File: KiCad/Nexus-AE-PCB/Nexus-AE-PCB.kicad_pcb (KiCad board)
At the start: 2 copper layers, 50 x 100 mm, 163 parts, among them CN1 I2C_IN, CN2 I2C_OUT, J1 Conn_01x20_Socket, J2 Conn_01x20_Socket, J3 AE_BUS, J4 Inputs, J5 Outputs, J6 SPI, J7 SD_CONN, Q1 AO3401, Q2 2N3904, Q3 2N3904, SW1 SW_Push, SW2 SW_Push, U1 ATmega4809-A, U2 MCP6002T-I_MS, U3 Driver_LED_PCA9633PW,118, U4 MCP6002T-I_MS, U5 MCP6002T-I_MS, U6 MCP6002T-I_MS, U7 USBLC6-2SC6, U8 MCP6002T-I_MS, U9 74xGxx_MDD_74AHCT1G125GV

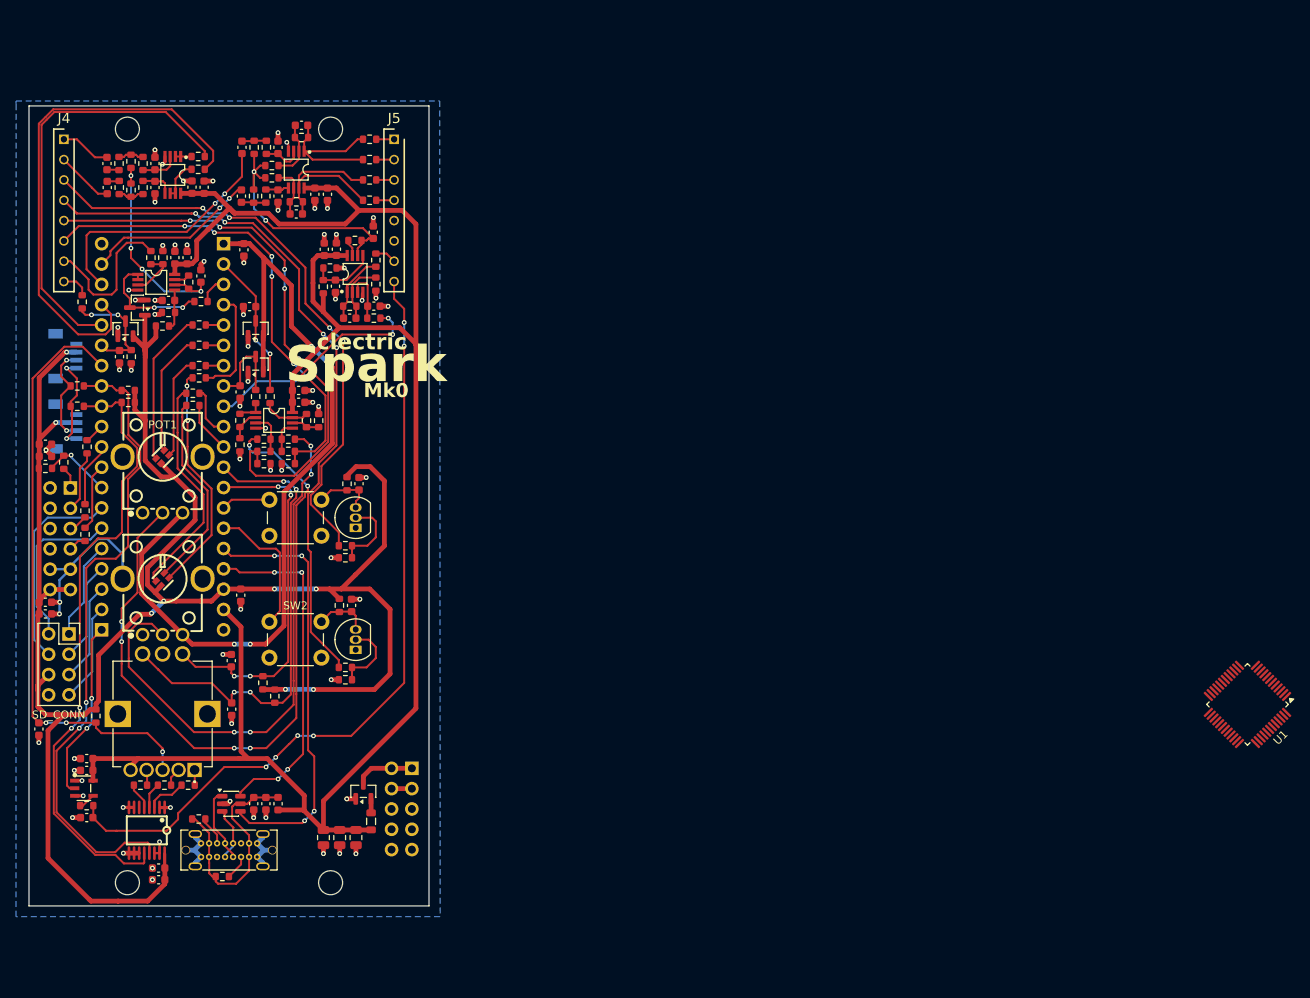
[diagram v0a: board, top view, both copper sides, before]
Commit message: PCB and schmeatic are both approx 90% complete
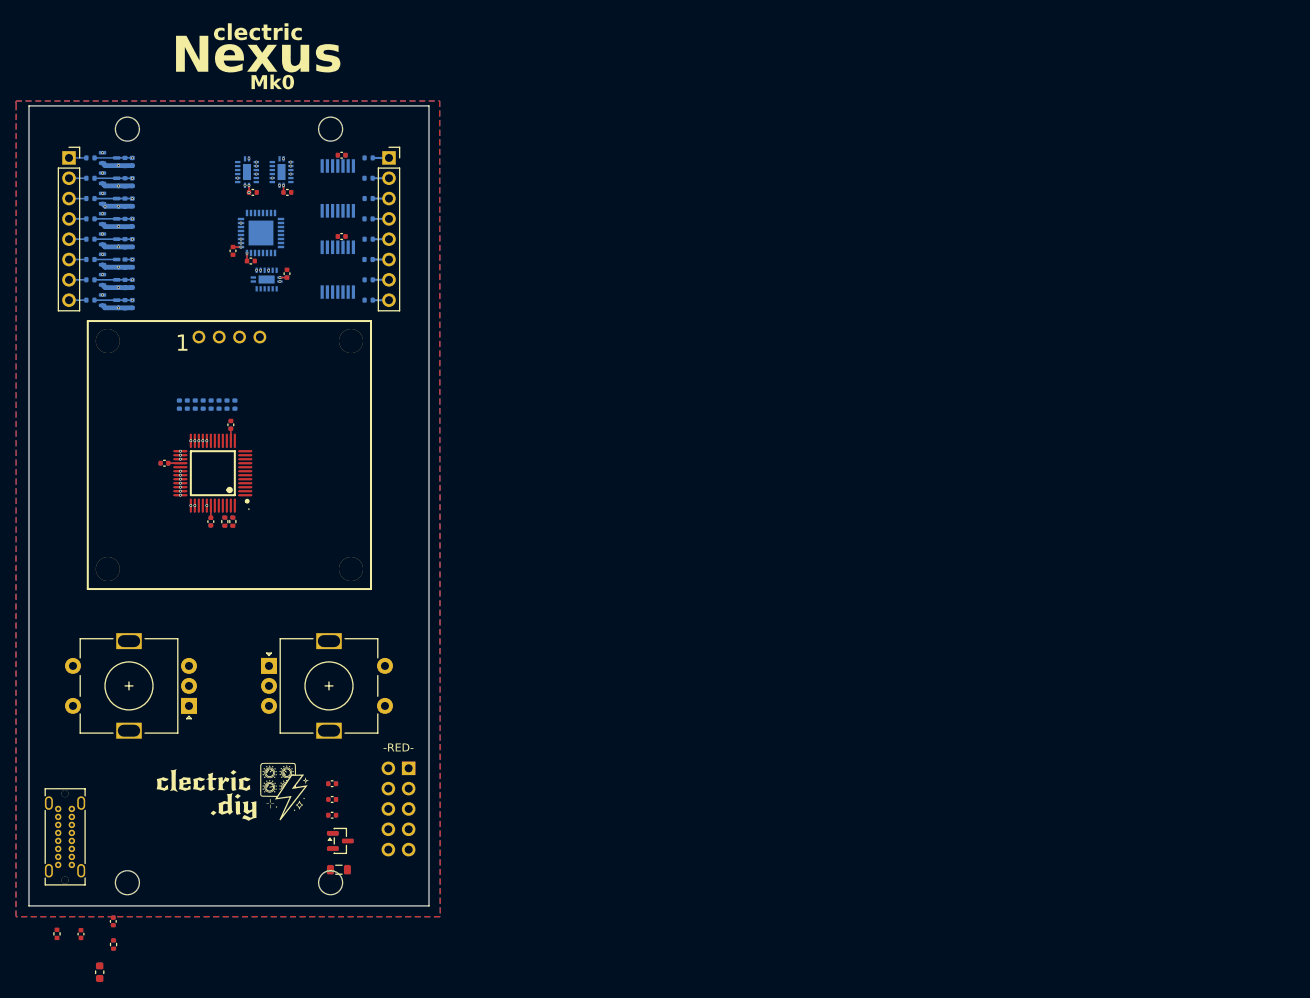
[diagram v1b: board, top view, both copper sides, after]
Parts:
- removed C24, C30, C36, C40, C42, C45, C50, C52: 10uF, Capacitor_SMD:C_0603_1608Metric
- removed C25, C26, C38: 1nF, Capacitor_SMD:C_0603_1608Metric
- removed C27, C28: 680pF, Capacitor_SMD:C_0603_1608Metric
- removed C29, C33, C34, C35, C39, C41, C43, C44, C48, C49, C51: 100nF, Capacitor_SMD:C_0603_1608Metric
- removed C37: 10nF, Capacitor_SMD:C_0603_1608Metric
- removed C46: 100pF, Capacitor_SMD:C_0603_1608Metric
- removed C47: 10pF, Capacitor_SMD:C_0603_1608Metric
- removed CN1: I2C_IN, clectric-diy:Connector_JST_BM04B-SRSS-TBT-LF-SN
- removed CN2: I2C_OUT, clectric-diy:Connector_JST_BM04B-SRSS-TBT-LF-SN
- removed J4: Inputs, clectric-diy:Connector_PinSocket-1x08-P2.54mm-H8.5mm_Preci-Dip_801-87-008-10-005101
- removed J5: Outputs, clectric-diy:Connector_PinSocket-1x08-P2.54mm-H8.5mm_Preci-Dip_801-87-008-10-005101
- removed J6: SPI, Connector_PinHeader_2.54mm:PinHeader_2x06_P2.54mm_Vertical
- removed J7: SD_CONN, Connector_PinSocket_2.54mm:PinSocket_2x04_P2.54mm_Vertical
- removed LED1, LED2: A-SP1943B1GHR6C-C01-2T, clectric-diy:LED_ARGB_Amicc_A-SP1943B1GHR6C-C01-2T
- removed POT1, POT2: RK09K1130D62, clectric-diy:Potentiometer_THT_Alps_RK09K1130D62
- removed Q2, Q3: 2N3904, Package_TO_SOT_THT:TO-92_Inline
- removed R37, R38, R43, R44, R45, R46, R55, R65, R68, R72, R78: 10K, Resistor_SMD:R_0603_1608Metric
- removed R39, R40, R49, R50, R51, R52, R63, R69, R75: 1K, Resistor_SMD:R_0603_1608Metric
- removed R41, R42, R53, R54, R70, R71: 100K, Resistor_SMD:R_0603_1608Metric
- removed R47, R48: 15K, Resistor_SMD:R_0603_1608Metric
- removed R56: 20K, Resistor_SMD:R_0603_1608Metric
- removed R62, R74, R76, R77: 100R, Resistor_SMD:R_0603_1608Metric
- removed R64, R67: 56K, Resistor_SMD:R_0603_1608Metric
- removed R66: 12.7K, Resistor_SMD:R_0603_1608Metric
- removed R73: 470R, Resistor_SMD:R_0603_1608Metric
- removed R79, R80, R81, R82: 47R, Resistor_SMD:R_0603_1608Metric
- removed SW1, SW2: SW_Push, Button_Switch_THT:SW_PUSH_6mm
- removed U8: MCP6002T-I_MS, clectric-diy:Amplifier_Operational_Microchip_MCP6002T-I_MS
- removed U9: 74xGxx_MDD_74AHCT1G125GV, clectric-diy:74xGxx_MDD_74AHCT1G125GV
- added D6: BAT54SW, Package_TO_SOT_SMD:SOT-323_SC-70, B.Cu at (88.5, 65.3)
- added D7: BAT54SW, Package_TO_SOT_SMD:SOT-323_SC-70, B.Cu at (88.5, 67.9)
- added D8: BAT54SW, Package_TO_SOT_SMD:SOT-323_SC-70, B.Cu at (88.5, 70.4)
- added ENC1: RotaryEncoder_Switch, Rotary_Encoder:RotaryEncoder_Alps_EC11E-Switch_Vertical_H20mm, F.Cu at (90.9, 118.6)
- added ENC2: RotaryEncoder_Switch, Rotary_Encoder:RotaryEncoder_Alps_EC11E-Switch_Vertical_H20mm, F.Cu at (115.9, 118.6)
- added OLED1: HS13L03W2C01, clectric-diy:OLED-TH_L35.4-W33.5_HS13L03W2C01, F.Cu at (103.4, 75.0)
- C1: value 100uF -> 100nF; footprint Capacitor_SMD:C_0805_2012Metric -> Capacitor_SMD:C_0402_1005Metric
- C10, C21, C5, C6: footprint Capacitor_SMD:C_0603_1608Metric -> Capacitor_SMD:C_0402_1005Metric
- C11, C7: value 10nF -> 100nF; footprint Capacitor_SMD:C_0603_1608Metric -> Capacitor_SMD:C_0402_1005Metric
- C12, C13, C14: value 10nF -> 100pF; footprint Capacitor_SMD:C_0603_1608Metric -> Capacitor_SMD:C_0402_1005Metric; moved to B.Cu
- C15: value 10uF -> 100pF; footprint Capacitor_SMD:C_0603_1608Metric -> Capacitor_SMD:C_0402_1005Metric; moved to B.Cu
- C16: value 100nF -> 100pF; footprint Capacitor_SMD:C_0603_1608Metric -> Capacitor_SMD:C_0402_1005Metric; moved to B.Cu
- C17, C18: value 1uF -> 100pF; footprint Capacitor_SMD:C_0603_1608Metric -> Capacitor_SMD:C_0402_1005Metric; moved to B.Cu
- C19: value 220pF -> 100pF; footprint Capacitor_SMD:C_0603_1608Metric -> Capacitor_SMD:C_0402_1005Metric; moved to B.Cu
- C2: value 10uF -> 100nF; footprint Capacitor_SMD:C_0805_2012Metric -> Capacitor_SMD:C_0402_1005Metric
- C20: value 220pF -> 100nF; footprint Capacitor_SMD:C_0603_1608Metric -> Capacitor_SMD:C_0402_1005Metric
- C22, C23, C9: value 10uF -> 100nF; footprint Capacitor_SMD:C_0603_1608Metric -> Capacitor_SMD:C_0402_1005Metric
- C3: footprint Capacitor_SMD:C_0805_2012Metric -> Capacitor_SMD:C_0402_1005Metric
- C4: value 10uF -> 100uF; footprint Capacitor_SMD:C_0603_1608Metric -> Capacitor_SMD:C_0402_1005Metric
- C8: value 100nF -> 10uF; footprint Capacitor_SMD:C_0603_1608Metric -> Capacitor_SMD:C_0402_1005Metric
- D1, D2, D4, D5: value BAT54S -> BAT54SW; footprint Package_TO_SOT_SMD:SOT-23 -> Package_TO_SOT_SMD:SOT-323_SC-70; moved to B.Cu
- D3: value RotaryEncoder_Switch_Bourns_PEL12T-4225S-S1024 -> BAT54SW; footprint clectric-diy:RotaryEncoder_Switch_Bourns_PEL12T-4225S-S1024 -> Package_TO_SOT_SMD:SOT-323_SC-70; moved to B.Cu
- G***: moved to F.Cu
- J1: value Conn_01x20_Socket -> AE_BUS; footprint clectric-diy:Connector_PinSocket-1x20-P2.54mm-H1.27mm_Mill-Max_315-13-120-41-004000 -> Connector_PinHeader_2.54mm:PinHeader_2x05_P2.54mm_Vertical
- J2: value Conn_01x20_Socket -> Conn_01x08_Socket; footprint clectric-diy:Connector_PinSocket-1x20-P2.54mm-H1.27mm_Mill-Max_315-13-120-41-004000 -> Connector_PinSocket_2.54mm:PinSocket_1x08_P2.54mm_Vertical; moved to F.Cu
- J3: value AE_BUS -> Conn_01x08_Socket; footprint Connector_PinHeader_2.54mm:PinHeader_2x05_P2.54mm_Vertical -> Connector_PinSocket_2.54mm:PinSocket_1x08_P2.54mm_Vertical; moved to F.Cu
- R1, R11, R13, R19, R2, R23, R3, R31, R7: value 10K -> 1k; footprint Resistor_SMD:R_0603_1608Metric -> Resistor_SMD:R_0402_1005Metric; moved to B.Cu
- R10: value 47R -> 56K; footprint Resistor_SMD:R_0603_1608Metric -> Resistor_SMD:R_0402_1005Metric
- R12, R24: value 1K -> 100k; footprint Resistor_SMD:R_0603_1608Metric -> Resistor_SMD:R_0402_1005Metric; moved to B.Cu
- R14, R21: value 100K -> 100k; footprint Resistor_SMD:R_0603_1608Metric -> Resistor_SMD:R_0402_1005Metric; moved to B.Cu
- R15, R22, R25, R26: value 10K -> 100k; footprint Resistor_SMD:R_0603_1608Metric -> Resistor_SMD:R_0402_1005Metric; moved to B.Cu
- R16: value 47R -> 100k; footprint Resistor_SMD:R_0603_1608Metric -> Resistor_SMD:R_0402_1005Metric; moved to B.Cu
- R17: value 330R -> 1k; footprint Resistor_SMD:R_0603_1608Metric -> Resistor_SMD:R_0402_1005Metric; moved to B.Cu
- R18, R8: value 47R -> 1k; footprint Resistor_SMD:R_0603_1608Metric -> Resistor_SMD:R_0402_1005Metric; moved to B.Cu
- R20, R35, R36, R4, R5, R6: value 100K -> 1k; footprint Resistor_SMD:R_0603_1608Metric -> Resistor_SMD:R_0402_1005Metric; moved to B.Cu
- R27: value 4K7 -> 4.7k; footprint Resistor_SMD:R_0603_1608Metric -> Resistor_SMD:R_0402_1005Metric
- R28: value 680R -> 4.7k; footprint Resistor_SMD:R_0603_1608Metric -> Resistor_SMD:R_0402_1005Metric
- R29, R30: value 470R -> 1k; footprint Resistor_SMD:R_0603_1608Metric -> Resistor_SMD:R_0402_1005Metric; moved to B.Cu
- R32: value 4K7 -> 1k; footprint Resistor_SMD:R_0603_1608Metric -> Resistor_SMD:R_0402_1005Metric; moved to B.Cu
- R33, R34: value 150K -> 1k; footprint Resistor_SMD:R_0603_1608Metric -> Resistor_SMD:R_0402_1005Metric; moved to B.Cu
- R9: value 330R -> 56K; footprint Resistor_SMD:R_0603_1608Metric -> Resistor_SMD:R_0402_1005Metric
- U1: value ATmega4809-A -> ATMEGA4809-AUR; footprint Package_QFP:TQFP-48_7x7mm_P0.5mm -> clectric-diy:TQFP-48_L7.0-W7.0-P0.50-LS9.0-BL
- U2, U4: value MCP6002T-I_MS -> 74HC4053BQ,115; footprint clectric-diy:Amplifier_Operational_Microchip_MCP6002T-I_MS -> clectric-diy:DHVQFN-16_L3.5-W2.5-P0.50-BL-EP; moved to B.Cu
- U3: value Driver_LED_PCA9633PW,118 -> 74HC4053BQ,115; footprint clectric-diy:TSSOP-16_L5.0-W4.4-P0.64-LS6.4-BL -> clectric-diy:DHVQFN-16_L3.5-W2.5-P0.50-BL-EP; moved to B.Cu
- U5: value MCP6002T-I_MS -> ADG2188BCPZ-REEL7; footprint clectric-diy:Amplifier_Operational_Microchip_MCP6002T-I_MS -> clectric-diy:LFCSP-32_L5.0-W5.0-P0.50-TL-EP3.1; moved to B.Cu
- U6: value MCP6002T-I_MS -> MCP6004T-I/ST; footprint clectric-diy:Amplifier_Operational_Microchip_MCP6002T-I_MS -> clectric-diy:TSSOP-14_L5.0-W4.4-P0.65-LS6.4-BL; moved to B.Cu
- U7: value USBLC6-2SC6 -> MCP6004T-I/ST; footprint Package_TO_SOT_SMD:SOT-23-6 -> clectric-diy:TSSOP-14_L5.0-W4.4-P0.65-LS6.4-BL; moved to B.Cu
- moved U1 132.5 mm to (101.4, 92.0), turned to 90 degrees
- moved U3 84.0 mm to (109.9, 54.4), turned to 90 degrees
- moved C15 80.7 mm to (91.3, 60.7), turned to -90 degrees
- moved C16 79.7 mm to (91.3, 63.3), turned to -90 degrees
- moved R10 78.2 mm to (88.9, 151.0), turned to 90 degrees
- moved J3 76.4 mm to (123.4, 52.6), turned to 0 degrees
- moved R9 73.2 mm to (81.9, 149.6), turned to 90 degrees
- moved C7 70.6 mm to (84.9, 149.7), turned to 90 degrees
- moved C5 69.6 mm to (116.3, 132.8), turned to 0 degrees
- moved J1 69.5 mm to (125.8, 128.9)
- moved C8 68.9 mm to (88.9, 148.1), turned to 90 degrees
- moved U7 68.1 mm to (117.0, 66.6)
- moved C13 67.1 mm to (91.3, 55.7)
- moved C14 66.9 mm to (91.3, 58.2), turned to -90 degrees
- moved R15 66.7 mm to (86.1, 57.7)
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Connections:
- C1 pad 1: +5V -> GND
- C1 pad 2: GND -> +5VA
- C10 pad 1: SW2 -> +5V
- C11 pad 1: POT2 -> +5V
- C12 pad 1: ENC_A -> AE_IN_A
- C13 pad 1: ENC_B -> AE_IN_B
- C14 pad 1: GND -> AE_IN_C
- C14 pad 2: ENC_CLICK -> GND
- C15 pad 1: +3.3V -> AE_IN_D
- C16 pad 1: +3.3V -> AE_IN_E
- C17 pad 1: AUDIO_AE_IN_1 -> AE_IN_F
- C17 pad 2: Net-(C17-Pad2) -> GND
- C18 pad 1: AUDIO_AE_IN_2 -> AE_IN_G
- C18 pad 2: Net-(C18-Pad2) -> GND
- C19 pad 1: Net-(U4A-+) -> AE_IN_H
- C2 pad 1: +5V -> GND
- C2 pad 2: GND -> +5VA
- C20 pad 1: Net-(U4B-+) -> GND
- C20 pad 2: GND -> +5V
- C21 pad 1: GND -> +5V
- C21 pad 2: +5V -> GND
- C22 pad 1: GND -> +5V
- C22 pad 2: +5V -> GND
- C23 pad 1: Net-(C23-Pad1) -> +5VA
- C23 pad 2: AUDIO_OUT_1 -> GND
- C3 pad 1: +5V -> GND
- C3 pad 2: GND -> +5V
- C4 pad 1: GND -> +5V
- C4 pad 2: +3.3V -> GND
- C5 pad 1: GND -> +5V
- C5 pad 2: +3.3VA -> GND
- C6 pad 1: SW1 -> +5V
- C7 pad 1: POT1 -> Net-(C7-Pad1)
- C8 pad 1: +5V -> Net-(C7-Pad1)
- C9 pad 1: GND -> +5V
- C9 pad 2: +5V -> GND
- D1 pad 2: +3.3VA -> +5V
- D1 pad 3: POT1 -> AE_IN_A
- D2 pad 2: +3.3VA -> +5V
- D2 pad 3: POT2 -> AE_IN_B
- D3 pad 1: Net-(D3-Pad1) -> GND
- D3 pad 2: Net-(D3-Pad2) -> +5V
- D3 pad 3: ENC_CLICK -> AE_IN_C
- D4 pad 1: +3.3V -> GND
- D4 pad 2: GND -> +5V
- D4 pad 3: Net-(D4-COM) -> AE_IN_D
- D5 pad 2: +3.3V -> +5V
- D5 pad 3: D14 -> AE_IN_E
- F1 pad 2: Net-(U7-VBUS) -> Net-(C7-Pad1)
- J1 pad 1: +3.3VA -> /Power Regulation/VCC_RAW
- J1 pad 10: LED2_B -> unconnected-(J1-Pin_10-Pad10)
- J1 pad 2: POT2 -> /Power Regulation/VCC_RAW
- J1 pad 3: A1 -> GND
- J1 pad 4: LED2_R -> GND
- J1 pad 5: LED1_B -> unconnected-(J1-Pin_5-Pad5)
- J1 pad 6: LED1_G -> unconnected-(J1-Pin_6-Pad6)
- J1 pad 7: LED1_R -> unconnected-(J1-Pin_7-Pad7)
- J1 pad 8: POT1 -> unconnected-(J1-Pin_8-Pad8)
- J1 pad 9: A7 -> unconnected-(J1-Pin_9-Pad9)
- J2 pad 1: D0 -> AE_IN_A_RAW
- J2 pad 2: SD_D3 -> AE_IN_B_RAW
- J2 pad 3: SD_D2 -> AE_IN_C_RAW
- J2 pad 4: SD_D1 -> AE_IN_D_RAW
- J2 pad 5: SD_D0 -> AE_IN_E_RAW
- J2 pad 6: SD_CMD -> AE_IN_F_RAW
- J2 pad 7: SD_CK -> AE_IN_G_RAW
- J2 pad 8: SPI_CS -> AE_IN_H_RAW
- J3 pad 1: /Power Regulation/VCC_RAW -> AE_OUT_1
- J3 pad 2: /Power Regulation/VCC_RAW -> AE_OUT_2
- J3 pad 3: GND -> AE_OUT_3
- J3 pad 4: GND -> AE_OUT_4
- J3 pad 5: unconnected-(J3-Pin_5-Pad5) -> AE_OUT_5
- J3 pad 6: unconnected-(J3-Pin_6-Pad6) -> AE_OUT_6
- J3 pad 7: unconnected-(J3-Pin_7-Pad7) -> AE_OUT_7
- J3 pad 8: unconnected-(J3-Pin_8-Pad8) -> AE_OUT_8
- R1 pad 1: POT1_CV -> AE_OUT_1
- R1 pad 2: GND -> DEST_1_BUF
- R10 pad 1: LED1_B -> Net-(C7-Pad1)
- R10 pad 2: Net-(LED1-Pad4) -> Net-(USB1-CC2)
- R11 pad 1: Net-(U2A--) -> AE_IN_A_RAW
- R11 pad 2: Net-(R11-Pad2) -> AE_IN_A
- R12 pad 1: Net-(R11-Pad2) -> AE_IN_A
- R12 pad 2: POT1 -> GND
- R13 pad 1: POT2_CV -> AE_IN_B_RAW
- R13 pad 2: GND -> AE_IN_B
- R14 pad 1: Net-(U2B-+) -> AE_IN_B
- R14 pad 2: POT2_CV -> GND
- R15 pad 1: SW2_CV -> AE_IN_C_RAW
- R15 pad 2: Net-(Q3-B) -> AE_IN_C
- R16 pad 1: LED2_G -> AE_IN_C
- R16 pad 2: Net-(LED2-Pad1) -> GND
- R17 pad 1: LED2_R -> AE_IN_D_RAW
- R17 pad 2: Net-(LED2-Pad2) -> AE_IN_D
- R18 pad 1: LED2_B -> AE_IN_D
- R18 pad 2: Net-(LED2-Pad4) -> GND
- R19 pad 1: +3.3V -> AE_IN_E_RAW
- R19 pad 2: SW2 -> AE_IN_E
- R2 pad 1: SW1_CV -> AE_OUT_2
- R2 pad 2: Net-(Q2-B) -> DEST_2_BUF
- R20 pad 1: Net-(POT2-Pad2) -> AE_IN_E
- R20 pad 2: Net-(U2B-+) -> GND
- R21 pad 1: Net-(Q3-B) -> AE_IN_F_RAW
- R21 pad 2: GND -> AE_IN_F
- R22 pad 1: Net-(U2B--) -> AE_IN_F
- R23 pad 1: Net-(U2B--) -> AE_IN_G_RAW
- R23 pad 2: Net-(R23-Pad2) -> AE_IN_G
- R24 pad 1: Net-(R23-Pad2) -> AE_IN_G
- R24 pad 2: POT2 -> GND
- R25 pad 1: +3.3V -> AE_IN_H_RAW
- R25 pad 2: ENC_A -> AE_IN_H
- R26 pad 1: +3.3V -> AE_IN_H
- R26 pad 2: ENC_B -> GND
- R27 pad 1: +3.3V -> +5V
- R28 pad 1: Net-(D3-Pad1) -> +5V
- R28 pad 2: ENC_LED_RED -> I2C_SCL
- R29 pad 1: Net-(D3-Pad2) -> MCU_GEN_A
- R29 pad 2: ENC_LED_GREEN -> /Microchip ATMega4809/MCU_GEN_A_RAW
- R3 pad 1: +3.3V -> AE_OUT_3
- R3 pad 2: SW1 -> DEST_3_BUF
- R30 pad 1: ENC_LED_BLUE -> MCU_GEN_B
- R30 pad 2: Net-(D3-Pad4) -> /Microchip ATMega4809/MCU_GEN_B_RAW
- R31 pad 1: +3.3V -> MCU_GEN_C
- R31 pad 2: ENC_CLICK -> /Microchip ATMega4809/MCU_GEN_C_RAW
- R32 pad 1: +3.3V -> MCU_GEN_D
- R32 pad 2: I2C_SCL -> /Microchip ATMega4809/MCU_GEN_D_RAW
- R33 pad 1: Net-(C17-Pad2) -> MCU_GEN_E
- R33 pad 2: Net-(R33-Pad2) -> /Microchip ATMega4809/MCU_GEN_E_RAW
- R34 pad 1: Net-(C18-Pad2) -> MCU_GEN_F
- R34 pad 2: Net-(R34-Pad2) -> /Microchip ATMega4809/MCU_GEN_F_RAW
- R35 pad 1: Net-(R33-Pad2) -> MCU_GEN_G
- R35 pad 2: VREF_1V65 -> /Microchip ATMega4809/MCU_GEN_G_RAW
- R36 pad 1: Net-(R34-Pad2) -> MCU_GEN_H
- R36 pad 2: VREF_1V65 -> /Microchip ATMega4809/MCU_GEN_H_RAW
- R4 pad 1: Net-(U2A-+) -> AE_OUT_4
- R4 pad 2: POT1_CV -> DEST_4_BUF
- R5 pad 1: Net-(Q2-B) -> AE_OUT_5
- R5 pad 2: GND -> DEST_5_BUF
- R6 pad 1: Net-(POT1-Pad2) -> AE_OUT_6
- R6 pad 2: Net-(U2A-+) -> DEST_6_BUF
- R7 pad 1: Net-(U2A--) -> AE_OUT_7
- R7 pad 2: GND -> DEST_7_BUF
- R8 pad 1: LED1_G -> AE_OUT_8
- R8 pad 2: Net-(LED1-Pad1) -> DEST_8_BUF
- R9 pad 1: LED1_R -> Net-(C7-Pad1)
- R9 pad 2: Net-(LED1-Pad2) -> Net-(USB1-CC1)
- U1 pad 10: unconnected-(U1-PC0-Pad10) -> /Microchip ATMega4809/MCU_GEN_A_RAW
- U1 pad 11: unconnected-(U1-PC1-Pad11) -> /Microchip ATMega4809/MCU_GEN_B_RAW
- U1 pad 12: unconnected-(U1-PC2-Pad12) -> /Microchip ATMega4809/MCU_GEN_C_RAW
- U1 pad 13: unconnected-(U1-PC3-Pad13) -> /Microchip ATMega4809/MCU_GEN_D_RAW
- U1 pad 16: unconnected-(U1-PC4-Pad16) -> /Microchip ATMega4809/MCU_GEN_E_RAW
- U1 pad 17: unconnected-(U1-PC5-Pad17) -> /Microchip ATMega4809/MCU_GEN_F_RAW
- U1 pad 18: unconnected-(U1-PC6-Pad18) -> /Microchip ATMega4809/MCU_GEN_G_RAW
- U1 pad 19: unconnected-(U1-PC7-Pad19) -> /Microchip ATMega4809/MCU_GEN_H_RAW
- U1 pad 20: AE_SOCKET_1 -> AE_IN_A
- U1 pad 21: AE_SOCKET_2 -> AE_IN_B
- U1 pad 22: AE_SOCKET_3 -> AE_IN_C
- U1 pad 23: AE_SOCKET_4 -> AE_IN_D
- U1 pad 24: AE_SOCKET_5 -> AE_IN_E
- U1 pad 25: AE_SOCKET_6 -> AE_IN_F
- U1 pad 26: AE_SOCKET_7 -> AE_IN_G
- U1 pad 27: AE_SOCKET_8 -> AE_IN_H
- U1 pad 30: unconnected-(U1-PE0-Pad30) -> SRC_SEL_A
- U1 pad 31: unconnected-(U1-PE1-Pad31) -> SRC_SEL_B
- U1 pad 32: unconnected-(U1-PE2-Pad32) -> SRC_SEL_C
- U1 pad 33: unconnected-(U1-PE3-Pad33) -> SRC_SEL_D
- U1 pad 34: unconnected-(U1-PF0-Pad34) -> SRC_SEL_E
- U1 pad 35: unconnected-(U1-PF1-Pad35) -> SRC_SEL_F
- U1 pad 36: unconnected-(U1-PF2-Pad36) -> SRC_SEL_G
- U1 pad 37: unconnected-(U1-PF3-Pad37) -> SRC_SEL_H
- U1 pad 38: unconnected-(U1-PF4-Pad38) -> MATRIX_RESET
- U1 pad 4: unconnected-(U1-PB0-Pad4) -> ENC_1_A
- U1 pad 41: unconnected-(U1-UPDI-Pad41) -> UPDI
- U1 pad 42: +5V -> +5VA
- U1 pad 46: unconnected-(U1-PA2-Pad46) -> I2C_SDA
- U1 pad 47: unconnected-(U1-PA3-Pad47) -> I2C_SCL
- U1 pad 5: unconnected-(U1-PB1-Pad5) -> ENC_1_B
- U1 pad 6: unconnected-(U1-PB2-Pad6) -> ENC_1_SW
- U1 pad 7: unconnected-(U1-PB3-Pad7) -> ENC_2_A
- U1 pad 8: unconnected-(U1-PB4-Pad8) -> ENC_2_B
- U1 pad 9: unconnected-(U1-PB5-Pad9) -> ENC_2_SW
- U2 pad 1: Net-(R11-Pad2) -> MCU_GEN_C
- U2 pad 2: Net-(U2A--) -> AE_IN_C
- U2 pad 3: Net-(U2A-+) -> MCU_GEN_B
- U2 pad 4: GND -> SRC_B
- U2 pad 5: Net-(U2B-+) -> AE_IN_B
- U2 pad 6: Net-(U2B--) -> GND
- U2 pad 7: Net-(R23-Pad2) -> GND
- U2 pad 8: +5V -> GND
- U3 pad 1: GND -> MCU_GEN_D
- U3 pad 10: GND -> SRC_SEL_E
- U3 pad 11: GND -> SRC_SEL_D
- U3 pad 12: I2C_SCL -> AE_IN_E
- U3 pad 13: I2C_SDA -> MCU_GEN_E
- U3 pad 14: GND -> SRC_E
- U3 pad 15: GND -> SRC_D
- U3 pad 16: +3.3V -> +5V
- U3 pad 2: GND -> AE_IN_D
- U3 pad 3: ENC_LED_RED -> MCU_GEN_F
- U3 pad 4: ENC_LED_GREEN -> SRC_F
- U3 pad 5: ENC_LED_BLUE -> AE_IN_F
- U3 pad 6: unconnected-(U3-LED3-Pad6) -> GND
- U3 pad 9: GND -> SRC_SEL_F
- U4 pad 1: Net-(U4A--) -> MCU_GEN_G
- U4 pad 2: Net-(U4A--) -> AE_IN_G
- U4 pad 3: Net-(U4A-+) -> GND
- U4 pad 5: Net-(U4B-+) -> GND
- U4 pad 6: Net-(U4B--) -> GND
- U4 pad 7: Net-(U4B--) -> GND
- U4 pad 8: +5V -> GND
- U5 pad 1: Net-(C27-Pad1) -> GND
- U5 pad 2: Net-(U5A--) -> unconnected-(U5-DNC-Pad2)
- U5 pad 3: Net-(U5A-+) -> SRC_A
- U5 pad 4: GND -> SRC_B
- U5 pad 5: Net-(U5B-+) -> SRC_C
- U5 pad 6: Net-(U5B--) -> SRC_D
- U5 pad 7: Net-(C28-Pad1) -> SRC_E
- U5 pad 8: +5V -> SRC_F
- U6 pad 1: Net-(D4-COM) -> DEST_1_BUF
- U6 pad 2: Net-(D4-COM) -> DEST_1_BUF
- U6 pad 3: Net-(U6A-+) -> DEST_1
- U6 pad 4: GND -> +5V
- U6 pad 5: Net-(U6B-+) -> DEST_2
- U6 pad 6: VREF_1V65 -> DEST_2_BUF
- U6 pad 7: Net-(R62-Pad1) -> DEST_2_BUF
- U6 pad 8: +5V -> DEST_3_BUF
- U7 pad 1: Net-(U7-I/O1-Pad1) -> DEST_5_BUF
- U7 pad 2: GND -> DEST_5_BUF
- U7 pad 3: Net-(U7-I/O2-Pad3) -> DEST_5
- U7 pad 4: USB_D- -> +5V
- U7 pad 5: Net-(U7-VBUS) -> DEST_6
- U7 pad 6: USB_D+ -> DEST_6_BUF
- USB1 pad A4: Net-(U7-VBUS) -> Net-(C7-Pad1)
- USB1 pad A6: Net-(U7-I/O1-Pad1) -> Net-(USB1-D+-PadA6)
- USB1 pad A7: Net-(U7-I/O2-Pad3) -> Net-(USB1-D--PadA7)
- USB1 pad A9: Net-(U7-VBUS) -> Net-(C7-Pad1)
- USB1 pad B4: Net-(U7-VBUS) -> Net-(C7-Pad1)
- USB1 pad B6: Net-(U7-I/O1-Pad1) -> Net-(USB1-D+-PadA6)
- USB1 pad B7: Net-(U7-I/O2-Pad3) -> Net-(USB1-D--PadA7)
- USB1 pad B9: Net-(U7-VBUS) -> Net-(C7-Pad1)
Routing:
- net +3.3V: track 262.0 -> 0.00 mm, vias 8 -> 0
- net +5V: track 241.2 -> 5.17 mm, vias 0 -> 13
- net +3.3VA: track 105.3 -> 0.00 mm, vias 4 -> 0
- net D0_AE_OUT: track 100.0 -> 0.00 mm, vias 6 -> 0
- net Net-(POT1-Pad2): track 90.5 -> 0.00 mm, vias 6 -> 0
- net SW2_CV: track 87.8 -> 0.00 mm, vias 4 -> 0
- net I2C_SDA: track 80.2 -> 0.00 mm, vias 2 -> 1
- net I2C_SCL: track 78.0 -> 0.00 mm, vias 2 -> 1
- net GND: track 108.6 -> 30.8 mm, vias 70 -> 9
- net SW1_CV: track 74.6 -> 0.00 mm, vias 4 -> 0
- net ENC_CLICK: track 74.5 -> 0.00 mm, vias 3 -> 0
- net POT1_CV: track 70.9 -> 0.00 mm, vias 6 -> 0
- net Net-(POT2-Pad2): track 70.6 -> 0.00 mm, vias 4 -> 0
- net AUDIO_IN_2: track 63.7 -> 0.00 mm
- net POT2_CV: track 60.4 -> 0.00 mm, vias 6 -> 0
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- added copper zone on F.Cu, net GND
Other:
- board text added: "Nexus"
- board text removed: "Spark"
